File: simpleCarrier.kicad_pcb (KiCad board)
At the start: 6 copper layers, 101.7 x 100.9 mm, 146 parts, among them CN1 KH-CL0.5-H2.0-22PIN, CN2 KH-CL0.5-H2.0-22PIN, IC2 RT9187CGB, J1 USB_B, J10 Conn_01x03_Socket, J11 Conn_01x05_Socket, J12 Conn_01x01_Pin, J13 Conn_01x01_Pin, J14 Conn_01x01_Pin, J15 Conn_01x01_Pin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

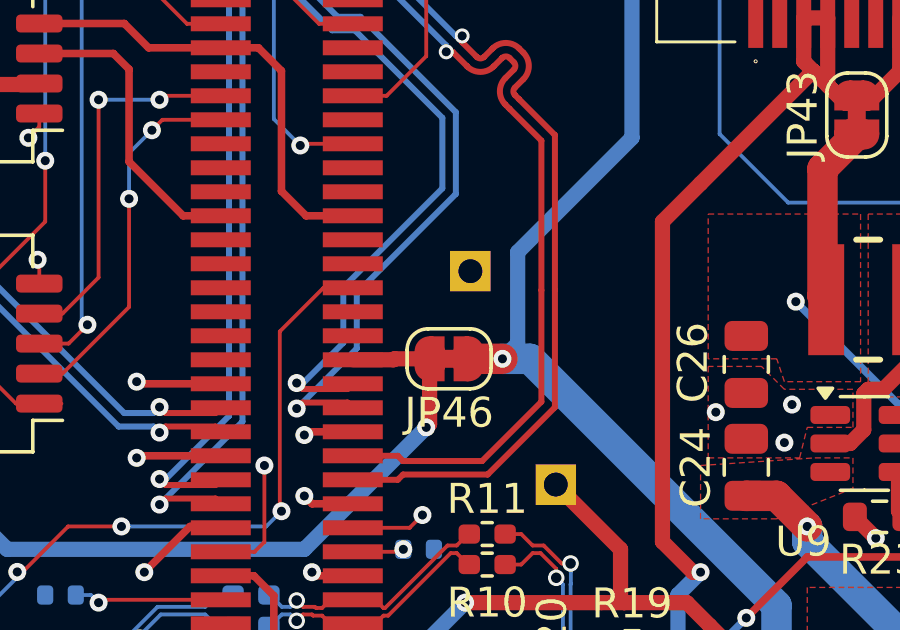
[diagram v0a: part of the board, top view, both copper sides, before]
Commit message: fixed unconnected test point for VCC 501
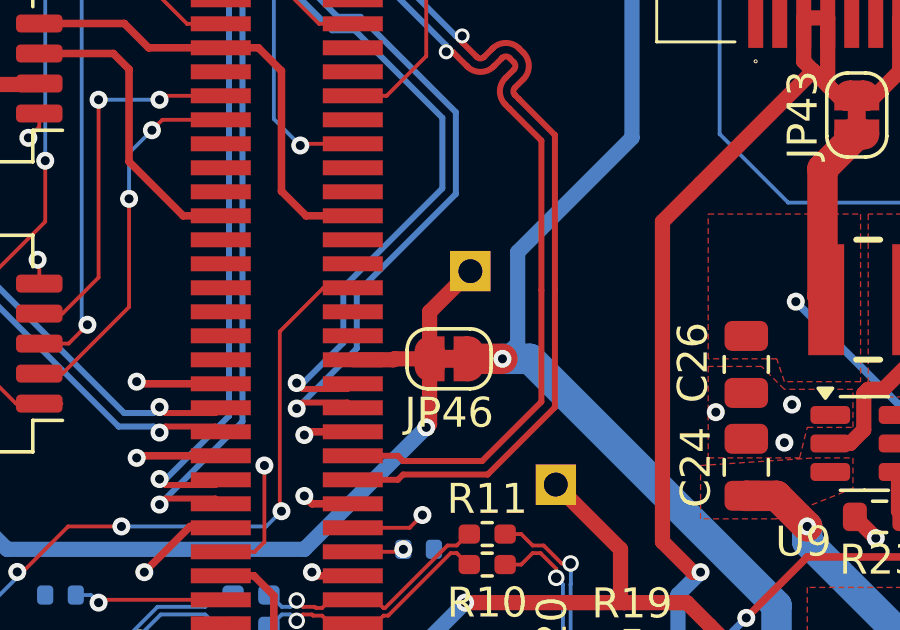
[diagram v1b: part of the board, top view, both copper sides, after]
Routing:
- net VCCO_PSIO_501: track 41.8 -> 45.3 mm
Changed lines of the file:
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@@
 		(tags "resistor handsolder")
 		(property "Reference" "R31"
-			(at -0.254 1.524 360)
+			(at -0.254 1.524 0)
 			(layer "F.SilkS")
 			(effects
@@
 		)
 		(property "Value" "R_0R_0402"
-			(at 0 1.17 360)
+			(at 0 1.17 0)
 			(layer "F.Fab")
 			(effects
@@
 		)
 		(fp_text user "${REFERENCE}"
-			(at 0 0 360)
+			(at 0 0 0)
 			(layer "F.Fab")
 			(effects
@@
 		(sheetname "connectors")
 		(sheetfile "connectors.kicad_sch")
-		(attr through_hole)
+		(attr through_hole dnp)
 		(fp_line
 			(start -7 3.15)
@@
 		(tags "Through hole angled pin header THT 1x01 2.00mm single row")
 		(property "Reference" "J15"
-			(at -0.127 1.778 -360)
+			(at -0.127 1.778 0)
 			(layer "B.SilkS")
 			(effects
@@
 		)
 		(property "Value" "Conn_01x01_Pin"
-			(at 3.1 -2 360)
+			(at 3.1 -2 0)
 			(layer "B.Fab")
 			(effects
@@
 		(tags "Through hole angled pin header THT 1x01 2.00mm single row")
 		(property "Reference" "J12"
-			(at -2.413 0.635 -360)
+			(at -2.413 0.635 0)
 			(layer "B.SilkS")
 			(effects
@@
 		)
 		(property "Value" "Conn_01x01_Pin"
-			(at 3.1 -2 360)
+			(at 3.1 -2 0)
 			(layer "B.Fab")
 			(effects
@@
 		(sheetname "PMOD")
 		(sheetfile "pmod.kicad_sch")
-		(attr through_hole)
+		(attr through_hole dnp)
 		(fp_line
 			(start 2.54 -7.62)
@@
 		(tags "Through hole angled pin header THT 1x01 2.00mm single row")
 		(property "Reference" "J14"
-			(at -1.524 -1.524 -0)
+			(at -1.524 -1.524 0)
 			(layer "B.SilkS")
 			(effects
@@
 		(tags "Through hole angled pin header THT 1x01 2.00mm single row")
 		(property "Reference" "J13"
-			(at -1.778 0 -180)
+			(at -1.778 0 180)
 			(layer "B.SilkS")
 			(effects
@@
 		)
 		(fp_text user "${REFERENCE}"
-			(at 2.25 0 360)
+			(at 2.25 0 0)
 			(layer "B.Fab")
 			(effects
@@
 		(sheetname "PMOD")
 		(sheetfile "pmod.kicad_sch")
-		(attr through_hole)
+		(attr through_hole dnp)
 		(fp_line
 			(start 2.54 -7.62)
@@
 		(tags "resistor handsolder")
 		(property "Reference" "R29"
-			(at 0 1.17 360)
+			(at 0 1.17 0)
 			(layer "B.SilkS")
 			(effects
@@
 		)
 		(property "Value" "R_0R_0402"
-			(at 0 -1.17 360)
+			(at 0 -1.17 0)
 			(layer "B.Fab")
 			(effects
@@
 		)
 		(fp_text user "${REFERENCE}"
-			(at 0 0 360)
+			(at 0 0 0)
 			(layer "B.Fab")
 			(effects
@@
 		(tags "Through hole angled pin header THT 1x01 2.00mm single row")
 		(property "Reference" "J17"
-			(at -0.127 1.778 -0)
+			(at -0.127 1.778 0)
 			(layer "B.SilkS")
 			(effects
@@
 		(tags "Through hole angled pin header THT 1x01 2.00mm single row")
 		(property "Reference" "J16"
-			(at -0.381 -1.651 -0)
+			(at -0.381 -1.651 0)
 			(layer "B.SilkS")
 			(effects
@@
 		(tags "Through hole angled pin header THT 1x01 2.00mm single row")
 		(property "Reference" "J18"
-			(at -0.075 -1.524 360)
+			(at -0.075 -1.524 0)
 			(layer "B.SilkS")
 			(effects
@@
 		)
 		(property "Value" "Conn_01x01_Pin"
-			(at 3.1 -2 360)
+			(at 3.1 -2 0)
 			(layer "B.Fab")
 			(effects
@@
 	)
 	(segment
+		(start 95.362 91.911)
+		(end 95.362 93.472)
+		(width 0.508)
+		(layer "F.Cu")
+		(net 329)
+	)
+	(segment
 		(start 95.362 95.646)
 		(end 95.25 95.758)
@@
 		(width 0.508)
 		(layer "F.Cu")
+		(net 329)
+	)
+	(segment
+		(start 96.722 90.551)
+		(end 95.362 91.911)
+		(width 0.508)
+		(layer "F.Cu")

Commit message: fixed jtag vref was not connected to 1.8V
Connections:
- C23 pad 1: MGTRAVTT -> +1V8
- J17 pad 1: MGTRAVTT -> +1V8
- JX3 pad 36: MGTRAVTT -> +1V8
- JX3 pad 42: MGTRAVTT -> +1V8
- L5 pad 2: MGTRAVTT -> +1V8
- R20 pad 1: MGTRAVTT -> +1V8
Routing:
- net +1V8: track 0.00 -> 80.0 mm, vias 0 -> 5
- net MGTRAVTT: track 41.9 -> 0.00 mm, vias 4 -> 0
- added copper zone on F.Cu, net +1V8
- removed copper zone on F.Cu, net MGTRAVTT
